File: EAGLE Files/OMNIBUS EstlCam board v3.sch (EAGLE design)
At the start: 67 parts, among them K1 691131710002, K2 691131710003, K3 691131710003, K4 691131710003, U1 LTV-847S, U2 L7805ACD2T-TR, U3 LM358M/NOPB, U4 LTV-847S, U5 PC817X3NSZ1B, U6 ULN2003AD, U7 L78L05ACU, U8 74AHC1G125

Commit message: PCB Bugfixes and polishing
• DRV Shield had an routing error (laser indicator LED) also R3 had a wrong value
• New Footprint for the 0.33uF Caps
• Silkscreen polishing
• almost all LEDs are 0805 package now
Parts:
- C4: value 220uf 25v -> 0.33uf 25v; device rcl:CPOL-EUE5-6 -> rcl:CPOL-EUE2-5
- D1: value (none) -> green; device SparkFun-LED:LED1206 -> led:LEDCHIPLED_0805

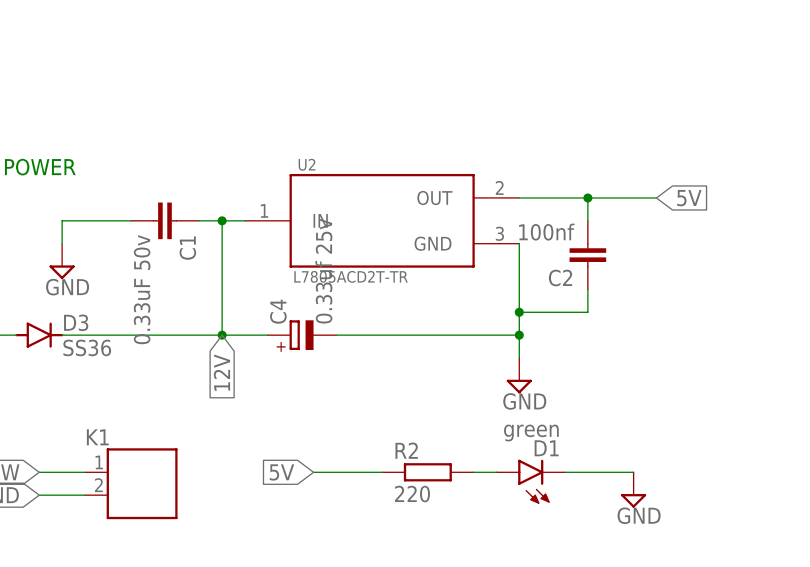
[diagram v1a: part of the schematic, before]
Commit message: Changed voltage regulators
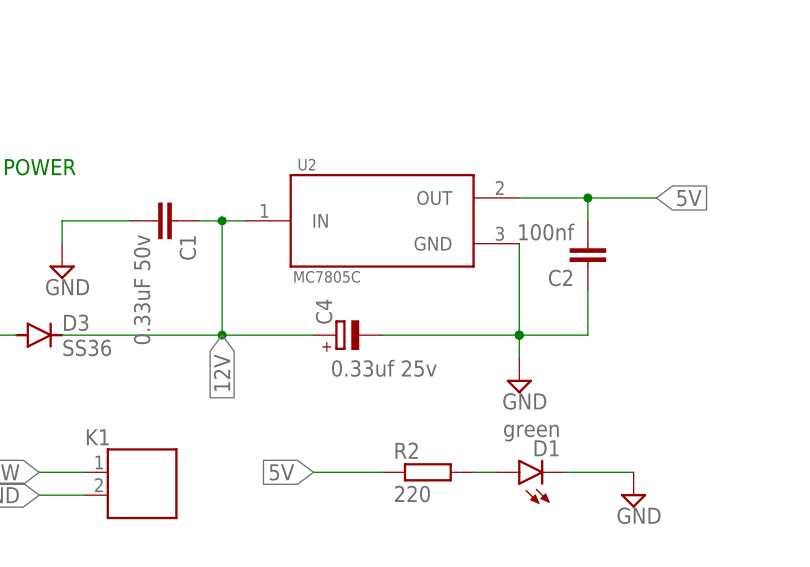
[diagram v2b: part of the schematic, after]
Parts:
- U2: value L7805ACD2T-TR -> MC7805C
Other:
- moved on the sheet: C4

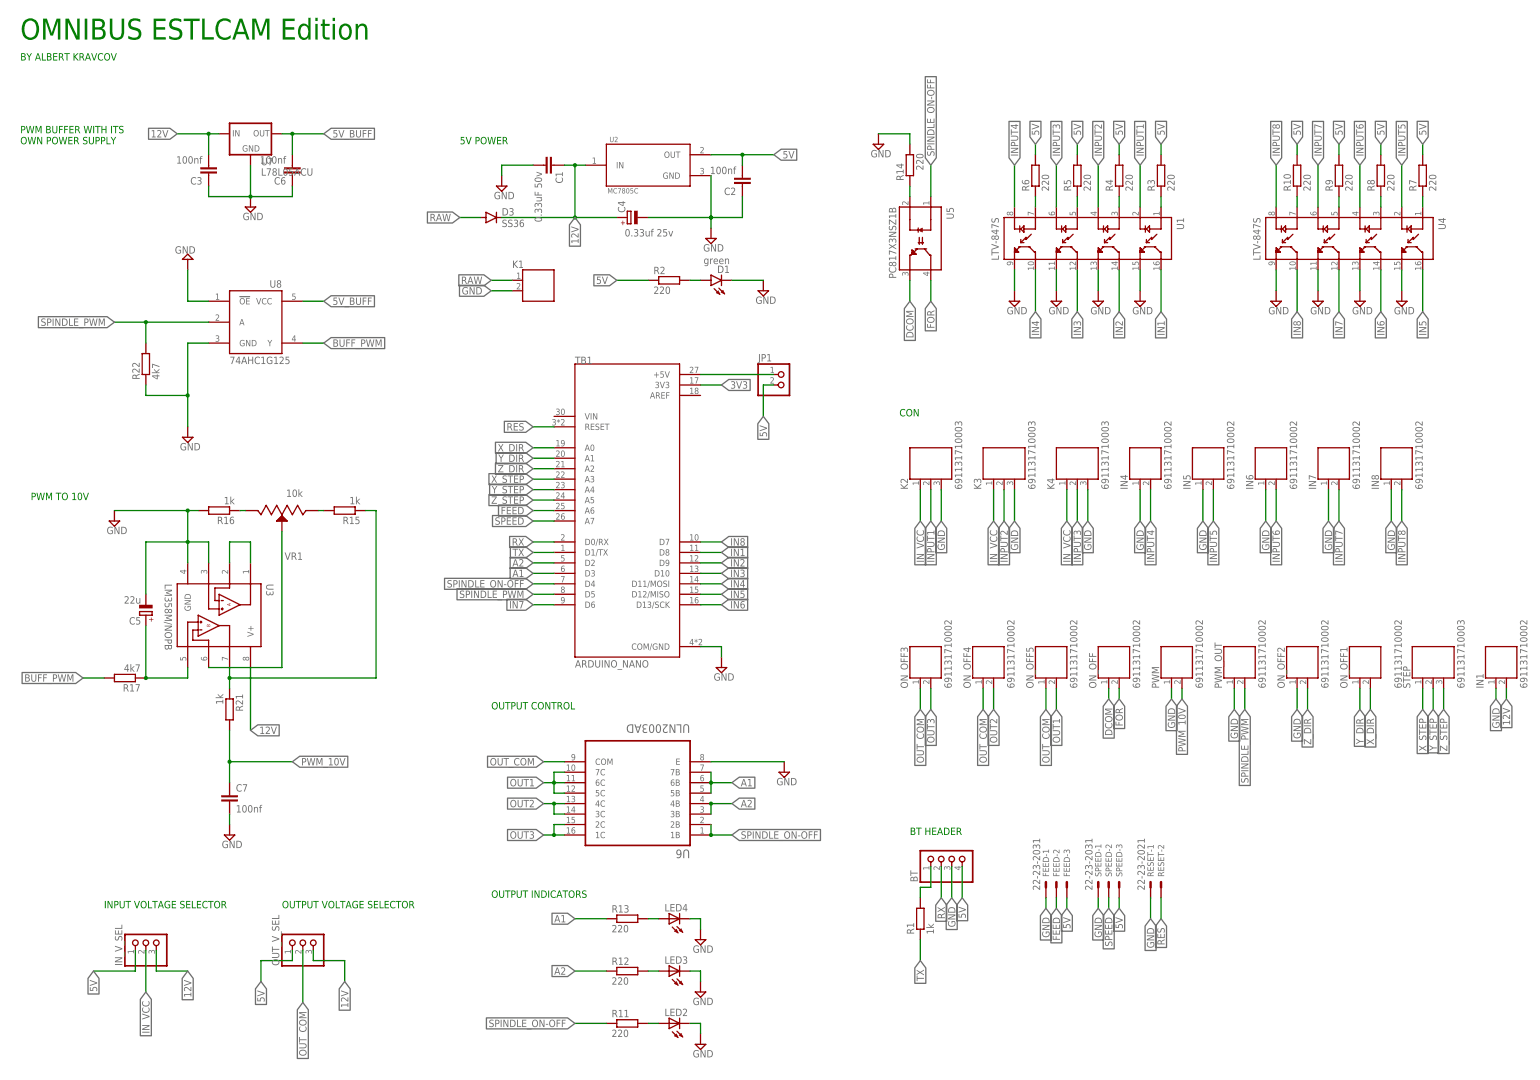
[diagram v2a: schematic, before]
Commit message: clean up
also added BOM
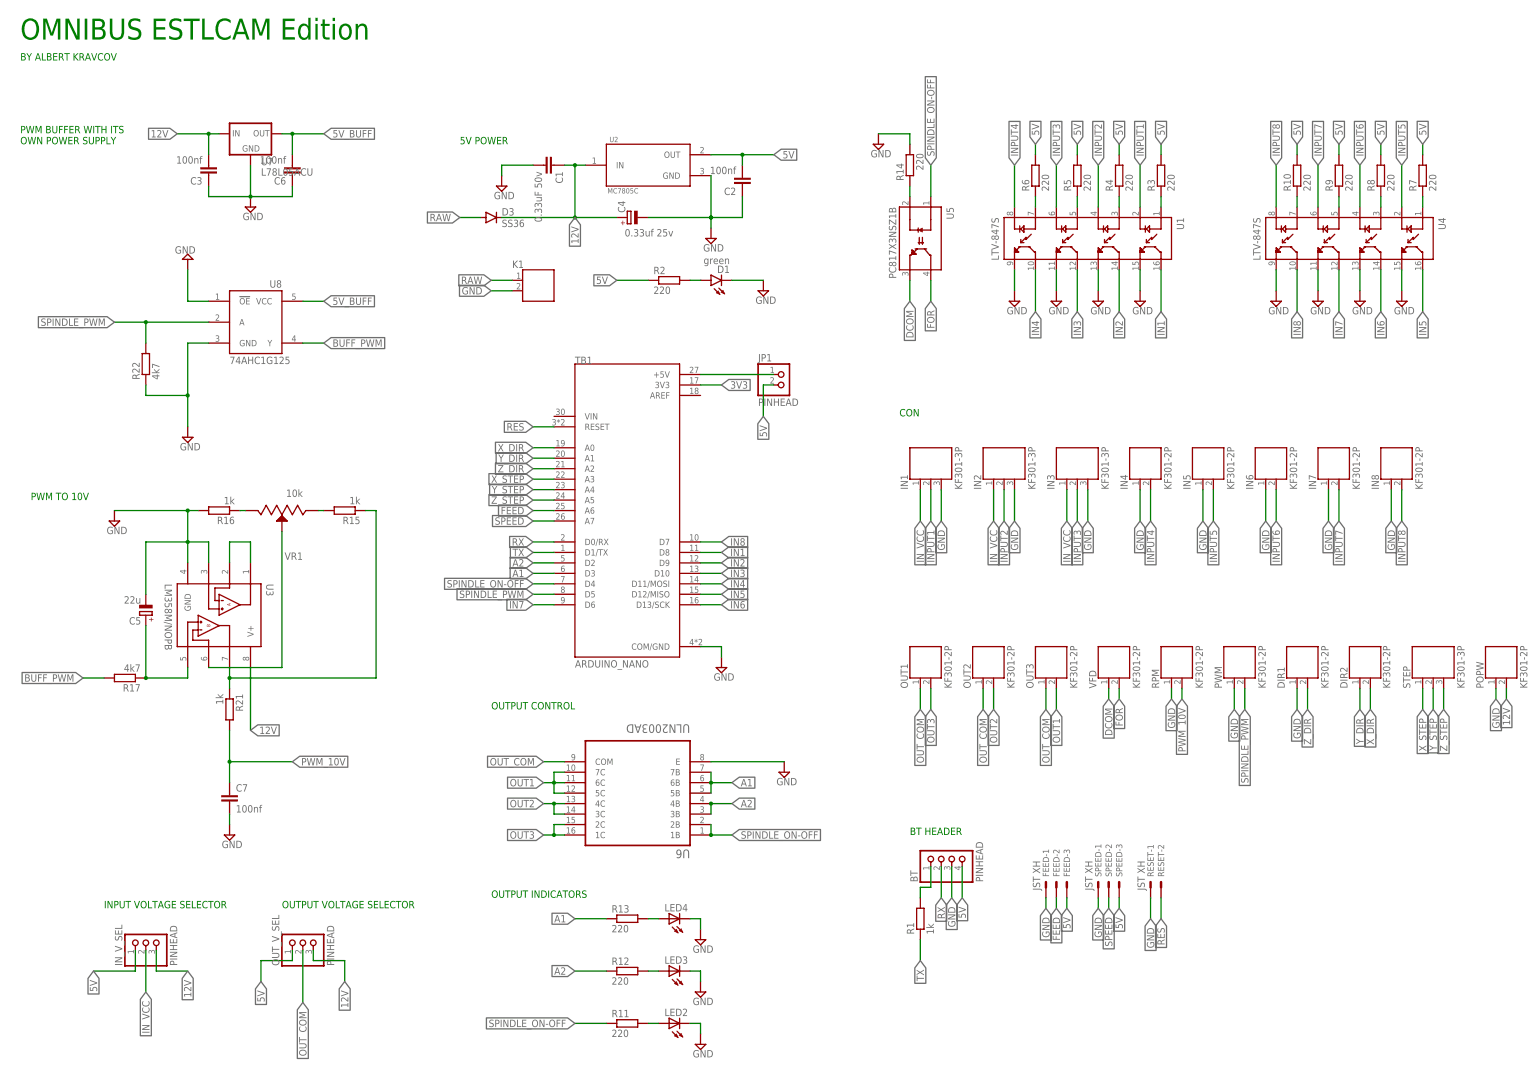
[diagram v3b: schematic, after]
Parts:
- removed K2: 691131710003, Wurth_Terminal_Blocks_Connectors_rev15d:691131710003
- removed PWM_OUT: 691131710002, Wurth_Terminal_Blocks_Connectors_rev15d:691131710002
- added POPW, RPM: KF301-2P, Wurth_Terminal_Blocks_Connectors_rev15d:691131710002
- BT, IN_V_SEL, JP1, OUT_V_SEL: value (none) -> PINHEAD
- DIR1, DIR2, IN4, IN5, IN6, IN7, IN8, OUT1, OUT2, OUT3, PWM, VFD: value 691131710002 -> KF301-2P
- FEED, SPEED: value 22-23-2031 -> JST XH
- IN1: value 691131710002 -> KF301-3P; device Wurth_Terminal_Blocks_Connectors_rev15d:691131710002 -> Wurth_Terminal_Blocks_Connectors_rev15d:691131710003
- IN2, IN3, STEP: value 691131710003 -> KF301-3P
- RESET: value 22-23-2021 -> JST XH
- renumbered K3 to IN2, K4 to IN3, ON_OFF to VFD, ON_OFF1 to DIR2, ON_OFF2 to DIR1, ON_OFF3 to OUT1, ON_OFF4 to OUT2, ON_OFF5 to OUT3
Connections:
- net 12V: now also POPW.2; no longer IN1.2
- net GND: now also IN1.3, POPW.1, RPM.1; no longer IN1.1, K2.3, PWM_OUT.1
- net INPUT1: now also IN1.2; no longer K2.2
- net IN_VCC: now also IN1.1; no longer K2.1
- net PWM_10V: now also RPM.2; no longer PWM.2
- net SPINDLE_PWM: now also PWM.2; no longer PWM_OUT.2
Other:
- moved on the sheet: PWM
